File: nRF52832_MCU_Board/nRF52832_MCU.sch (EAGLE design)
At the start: 55 parts, among them J1 TSW-103-02-S-S, J2 TSW-116-02-S-S, J3 TSW-116-02-S-S, J4 TSW-103-02-S-S, J5 MICROUSB, J6 DEBUG_CONNECTOR, J7 FPC_05P-RA-SMD, J8 MM8130-2600, U1 NRF52832, U2 TLV1117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

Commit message: Restructured MCU_Board
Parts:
- renumbered U$4 to BNT2, U$5 to BTN1
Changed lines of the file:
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@@
 <setting verticaltext="up"/>
 </settings>
-<grid distance="0.1" unitdist="inch" unit="inch" style="lines" multiple="1" display="yes" altdistance="0.01" altunitdist="inch" altunit="inch"/>
+<grid distance="0.1" unitdist="inch" unit="inch" style="lines" multiple="1" display="no" altdistance="0.01" altunitdist="inch" altunit="inch"/>
 <layers>
 <layer number="1" name="Top" color="4" fill="1" visible="no" active="no"/>
@@
 <part name="GND24" library="supply1" deviceset="GND" device=""/>
 <part name="BATT1" library="Nordic_misc" deviceset="CR1632" device=""/>
-<part name="U$4" library="Nordic_misc" deviceset="PANASONIC_EVQPT5A15" device=""/>
-<part name="U$5" library="Nordic_misc" deviceset="PANASONIC_EVQPT5A15" device=""/>
+<part name="BNT2" library="Nordic_misc" deviceset="PANASONIC_EVQPT5A15" device=""/>
+<part name="BTN1" library="Nordic_misc" deviceset="PANASONIC_EVQPT5A15" device=""/>
 <part name="R7" library="Nordic_misc" deviceset="RESISTOR" device="_0402_N" value="100k"/>
 <part name="R8" library="Nordic_misc" deviceset="RESISTOR" device="_0402_N" value="100k"/>
@@
 <instance part="GND24" gate="1" x="40.64" y="132.08" rot="MR0"/>
 <instance part="BATT1" gate="G$1" x="86.36" y="38.1"/>
-<instance part="U$4" gate="G$1" x="218.44" y="88.9"/>
-<instance part="U$5" gate="G$1" x="218.44" y="132.08"/>
+<instance part="BNT2" gate="G$1" x="218.44" y="88.9"/>
+<instance part="BTN1" gate="G$1" x="218.44" y="132.08"/>
 <instance part="R7" gate="R$1" x="208.28" y="106.68" rot="R90"/>
 <instance part="R8" gate="R$1" x="208.28" y="149.86" rot="R90"/>
@@
 </segment>
 <segment>
-<pinref part="U$4" gate="G$1" pin="GND"/>
+<pinref part="BNT2" gate="G$1" pin="GND"/>
 <pinref part="GND25" gate="1" pin="GND"/>
 </segment>
 <segment>
-<pinref part="U$4" gate="G$1" pin="B"/>
+<pinref part="BNT2" gate="G$1" pin="B"/>
 <wire x1="236.22" y1="99.06" x2="238.76" y2="99.06" width="0.1524" layer="91"/>
 <wire x1="238.76" y1="99.06" x2="238.76" y2="91.44" width="0.1524" layer="91"/>
-<pinref part="U$4" gate="G$1" pin="B'"/>
+<pinref part="BNT2" gate="G$1" pin="B'"/>
 <wire x1="238.76" y1="91.44" x2="238.76" y2="83.82" width="0.1524" layer="91"/>
 <wire x1="236.22" y1="91.44" x2="238.76" y2="91.44" width="0.1524" layer="91"/>
@@
 </segment>
 <segment>
-<pinref part="U$5" gate="G$1" pin="GND"/>
+<pinref part="BTN1" gate="G$1" pin="GND"/>
 <pinref part="GND27" gate="1" pin="GND"/>
 </segment>
 <segment>
-<pinref part="U$5" gate="G$1" pin="B"/>
+<pinref part="BTN1" gate="G$1" pin="B"/>
 <wire x1="236.22" y1="142.24" x2="238.76" y2="142.24" width="0.1524" layer="91"/>
 <wire x1="238.76" y1="142.24" x2="238.76" y2="134.62" width="0.1524" layer="91"/>
-<pinref part="U$5" gate="G$1" pin="B'"/>
+<pinref part="BTN1" gate="G$1" pin="B'"/>
 <wire x1="238.76" y1="134.62" x2="238.76" y2="127" width="0.1524" layer="91"/>
 <wire x1="236.22" y1="134.62" x2="238.76" y2="134.62" width="0.1524" layer="91"/>
@@
 <segment>
 <pinref part="R8" gate="R$1" pin="1"/>
-<pinref part="U$5" gate="G$1" pin="A"/>
+<pinref part="BTN1" gate="G$1" pin="A"/>
 <wire x1="208.28" y1="142.24" x2="208.28" y2="144.78" width="0.1524" layer="91"/>
 <wire x1="213.36" y1="142.24" x2="208.28" y2="142.24" width="0.1524" layer="91"/>
@@
 <net name="N$7" class="0">
 <segment>
-<pinref part="U$4" gate="G$1" pin="A'"/>
+<pinref part="BNT2" gate="G$1" pin="A'"/>
 <pinref part="R7" gate="R$1" pin="1"/>
 <wire x1="213.36" y1="91.44" x2="208.28" y2="91.44" width="0.1524" layer="91"/>
 <wire x1="208.28" y1="91.44" x2="208.28" y2="99.06" width="0.1524" layer="91"/>
-<pinref part="U$4" gate="G$1" pin="A"/>
+<pinref part="BNT2" gate="G$1" pin="A"/>
 <wire x1="208.28" y1="99.06" x2="208.28" y2="101.6" width="0.1524" layer="91"/>
 <wire x1="213.36" y1="99.06" x2="208.28" y2="99.06" width="0.1524" layer="91"/>

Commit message: Done some work in silk
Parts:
- removed BNT2: PANASONIC_EVQPT5A15, Nordic_misc:PANASONIC_EVQPT5A15
- removed J1, J4: TSW-103-02-S-S, con-samtec:TSW-103-02-S-S
- removed J2, J3: TSW-116-02-S-S, con-samtec:TSW-116-02-S-S
- added BTN2: PANASONIC_EVQPT5A15, Nordic_misc:PANASONIC_EVQPT5A15
- added U$1, U$2: HEADER_3X1, Nordic_misc:HEADER_3X1
- added U$3, U$4: HEADER_16X1, Nordic_misc:HEADER_16X1
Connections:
- net GND: now also BTN2.B, BTN2.B', BTN2.GND, U$1.1, U$2.3; no longer BNT2.B, BNT2.B', BNT2.GND, J1-3.1, J4-3.1
- net N$6: now also BTN2.A; no longer BTN1.A
- net N$7: now also BTN1.A, BTN1.A'; no longer BNT2.A, BNT2.A'
- net P0.00: now also U$4.8; no longer J3-9.1
- net P0.01: now also U$4.9; no longer J3-8.1
- net P0.02: now also U$4.10; no longer J3-7.1
- net P0.03: now also U$4.11; no longer J3-6.1
- net P0.04: now also U$4.12; no longer J3-5.1
- net P0.05: now also U$4.13; no longer J3-4.1
- net P0.06: now also U$4.14; no longer J3-3.1
- net P0.07: now also U$4.15; no longer J3-2.1
- net P0.08: now also U$4.16; no longer J3-1.1
- net P0.09: now also U$3.1; no longer J2-1.1
- net P0.10: now also U$3.2; no longer J2-2.1
- net P0.11: now also U$3.3; no longer J2-3.1
- net P0.12: now also U$3.4; no longer J2-4.1
- net P0.13: now also U$3.5; no longer J2-5.1
- net P0.14: now also U$3.6; no longer J2-6.1
- net P0.15: now also U$3.7; no longer J2-7.1
- net P0.16: now also U$3.8; no longer J2-8.1
- net P0.17: now also U$3.9; no longer J2-9.1
- net P0.18/SWO: now also U$3.10; no longer J2-10.1
- net P0.19: now also U$3.11; no longer J2-11.1
- net P0.20: now also U$3.12; no longer J2-12.1
- net P0.21/RESET: now also U$3.13; no longer J2-13.1
- net P0.22: now also U$3.14; no longer J2-14.1
- net P0.23: now also U$3.15; no longer J2-15.1
- net P0.24: now also U$3.16; no longer J2-16.1
- net P0.25: now also U$4.1; no longer J3-16.1
- net P0.26: now also U$4.2; no longer J3-15.1
- net P0.27: now also U$4.3; no longer J3-14.1
- net P0.28: now also U$4.4; no longer J3-13.1
- net P0.29: now also U$4.5; no longer J3-12.1
- net P0.30: now also U$4.6; no longer J3-11.1
- net P0.31: now also U$4.7; no longer J3-10.1
- net VDD_P3V3: now also U$1.2, U$2.2; no longer J1-2.1, J4-2.1
- net VDD_P5V0: now also U$1.3, U$2.1; no longer J1-1.1, J4-1.1
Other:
- moved on the sheet: BTN1, R5, R6, R7, R8

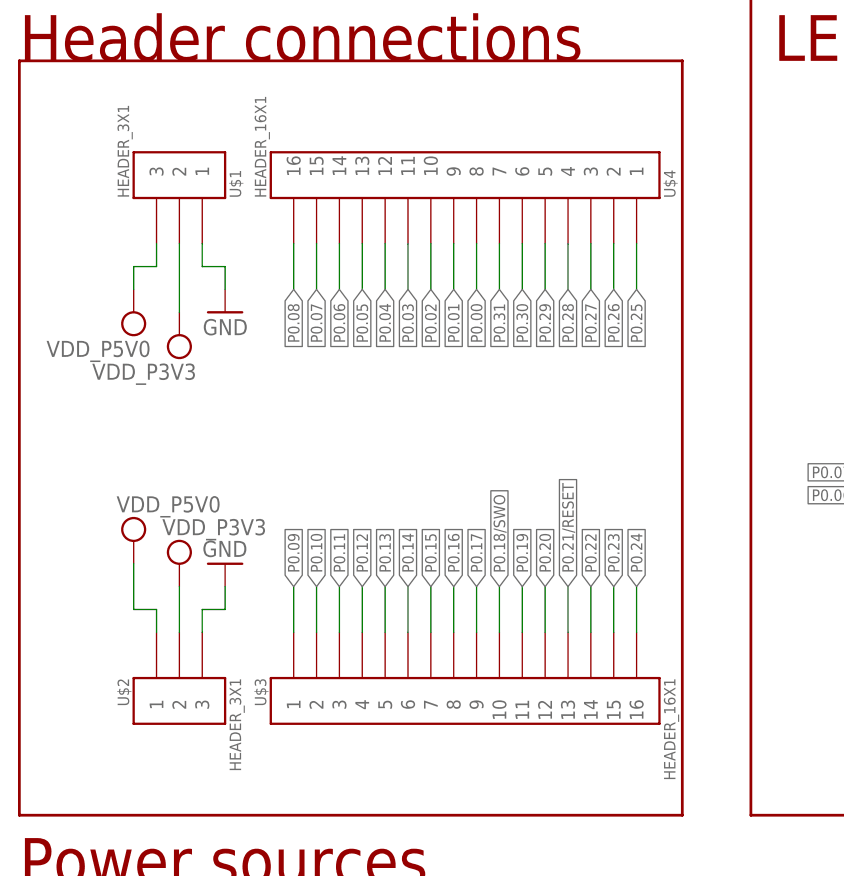
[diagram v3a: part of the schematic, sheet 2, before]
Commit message: Added name to headers in library, named headers properly
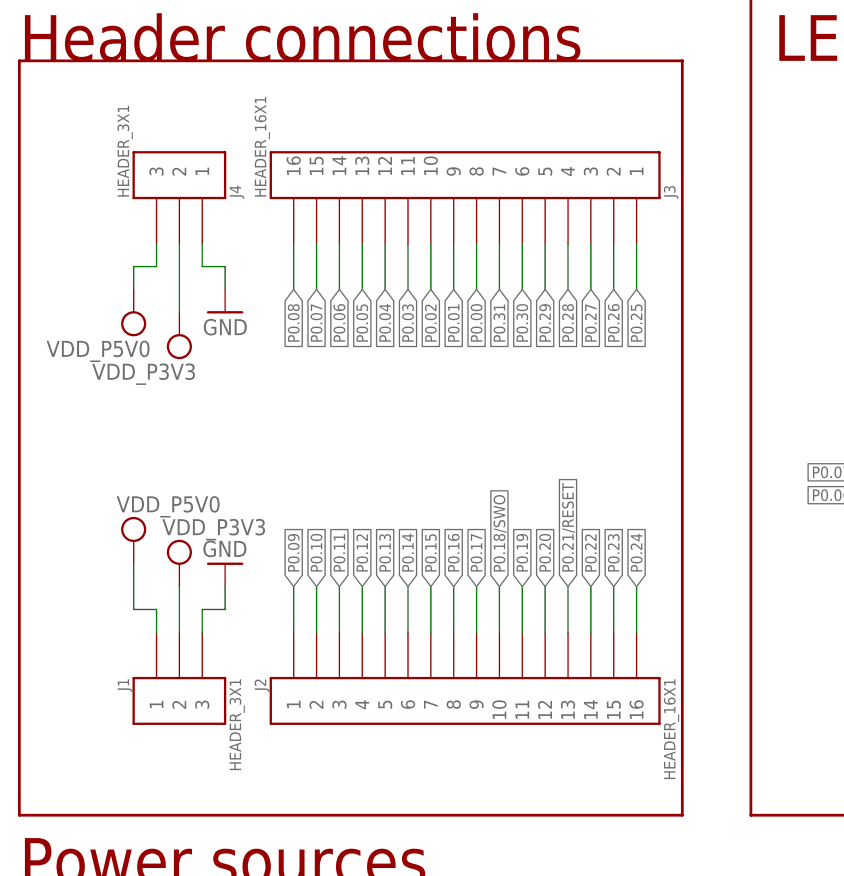
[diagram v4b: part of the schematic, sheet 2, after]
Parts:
- renumbered U$1 to J4, U$2 to J1, U$3 to J2, U$4 to J3

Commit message: Issue #3: Fixed wrong connections on P0.21/RESET - 6 and P0.18/SWO - 10
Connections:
- net P0.18/SWO: now also J6.6; no longer J6.10
- net P0.21/RESET: now also J6.10; no longer J6.6
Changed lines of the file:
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@@
 <segment>
 <pinref part="U1" gate="U$1" pin="P0.18/SWO@21"/>
-<wire x1="127" y1="55.88" x2="127" y2="40.64" width="0.1524" layer="91"/>
+<wire x1="127" y1="55.88" x2="127" y2="45.72" width="0.1524" layer="91"/>
 <label x="127" y="38.1" size="1.27" layer="95" rot="R270" xref="yes"/>
-<pinref part="J6" gate="G$1" pin="10"/>
+<wire x1="127" y1="45.72" x2="127" y2="40.64" width="0.1524" layer="91"/>
 <wire x1="127" y1="40.64" x2="127" y2="38.1" width="0.1524" layer="91"/>
-<wire x1="170.18" y1="40.64" x2="127" y2="40.64" width="0.1524" layer="91"/>
-<junction x="127" y="40.64"/>
-<label x="160.02" y="40.64" size="1.778" layer="95"/>
+<label x="154.94" y="45.72" size="1.778" layer="95"/>
+<pinref part="J6" gate="G$1" pin="6"/>
+<wire x1="170.18" y1="45.72" x2="127" y2="45.72" width="0.1524" layer="91"/>
+<junction x="127" y="45.72"/>
 </segment>
 </net>
@@
 <segment>
 <pinref part="U1" gate="U$1" pin="P0.19@22"/>
-<wire x1="129.54" y1="55.88" x2="129.54" y2="53.34" width="0.1524" layer="91"/>
-<label x="129.54" y="53.34" size="1.27" layer="95" rot="R270" xref="yes"/>
+<wire x1="129.54" y1="55.88" x2="129.54" y2="38.1" width="0.1524" layer="91"/>
+<label x="129.54" y="38.1" size="1.27" layer="95" rot="R270" xref="yes"/>
 </segment>
 </net>
@@
 <segment>
 <pinref part="U1" gate="U$1" pin="P0.20@23"/>
-<wire x1="132.08" y1="55.88" x2="132.08" y2="53.34" width="0.1524" layer="91"/>
-<label x="132.08" y="53.34" size="1.27" layer="95" rot="R270" xref="yes"/>
+<wire x1="132.08" y1="55.88" x2="132.08" y2="38.1" width="0.1524" layer="91"/>
+<label x="132.08" y="38.1" size="1.27" layer="95" rot="R270" xref="yes"/>
 </segment>
 </net>
@@
 <wire x1="134.62" y1="55.88" x2="134.62" y2="45.72" width="0.1524" layer="91"/>
 <label x="134.62" y="38.1" size="1.27" layer="95" rot="R270" xref="yes"/>
-<pinref part="J6" gate="G$1" pin="6"/>
-<wire x1="134.62" y1="45.72" x2="134.62" y2="38.1" width="0.1524" layer="91"/>
-<wire x1="170.18" y1="45.72" x2="134.62" y2="45.72" width="0.1524" layer="91"/>
-<junction x="134.62" y="45.72"/>
-<label x="160.02" y="45.72" size="1.778" layer="95"/>
+<wire x1="134.62" y1="45.72" x2="134.62" y2="40.64" width="0.1524" layer="91"/>
+<label x="154.94" y="40.64" size="1.778" layer="95"/>
+<pinref part="J6" gate="G$1" pin="10"/>
+<wire x1="134.62" y1="40.64" x2="134.62" y2="38.1" width="0.1524" layer="91"/>
+<wire x1="170.18" y1="40.64" x2="134.62" y2="40.64" width="0.1524" layer="91"/>
+<junction x="134.62" y="40.64"/>
 </segment>
 </net>
